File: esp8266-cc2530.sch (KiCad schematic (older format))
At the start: 34 parts, among them J1 CC2530_programmingHeader, J2 Conn_Coaxial, U1 WeMos_D1_mini, U2 AMS1117-3.3, U3 CC2530Fxxx, U4 RFX2401C, Y1 32.768kHz, Y2 32MHz

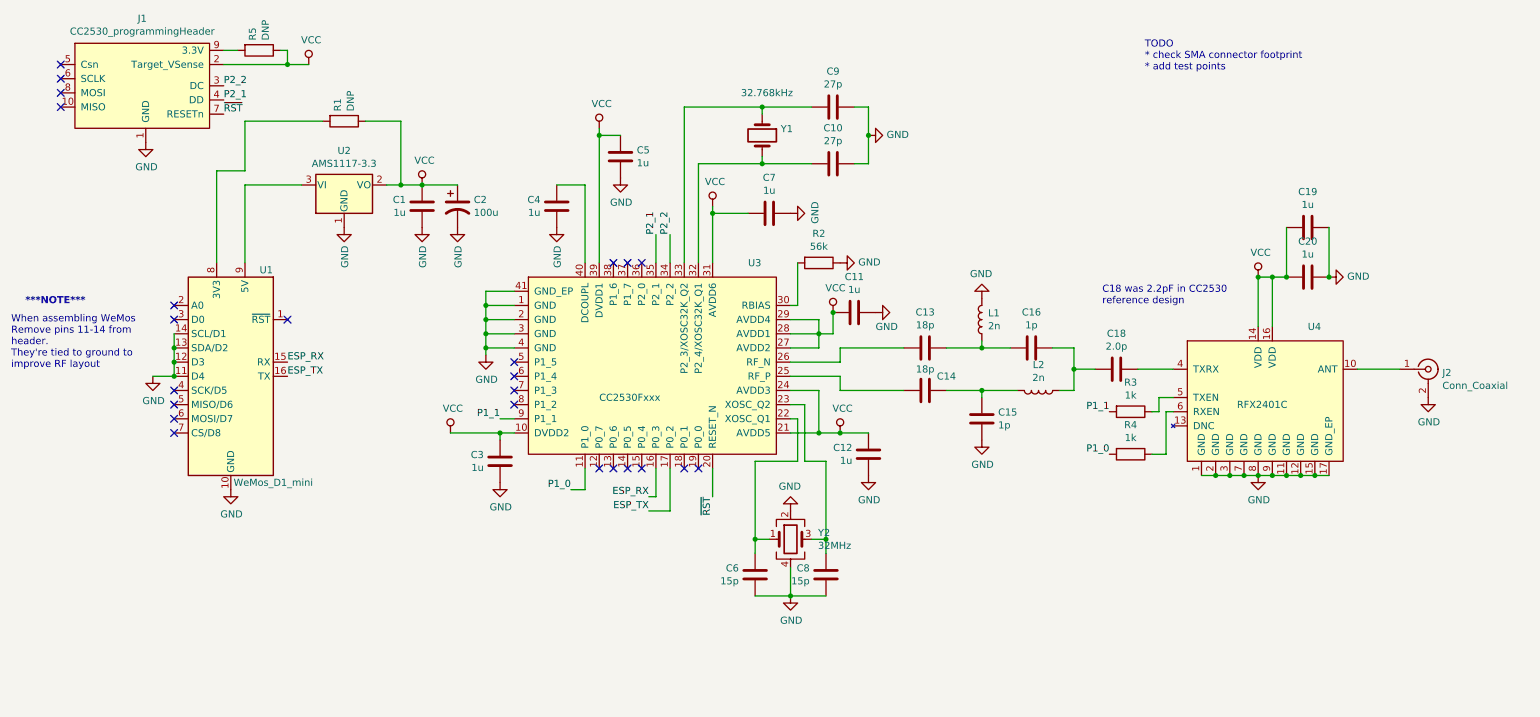
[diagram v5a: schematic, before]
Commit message: added usb connector, not routed yet
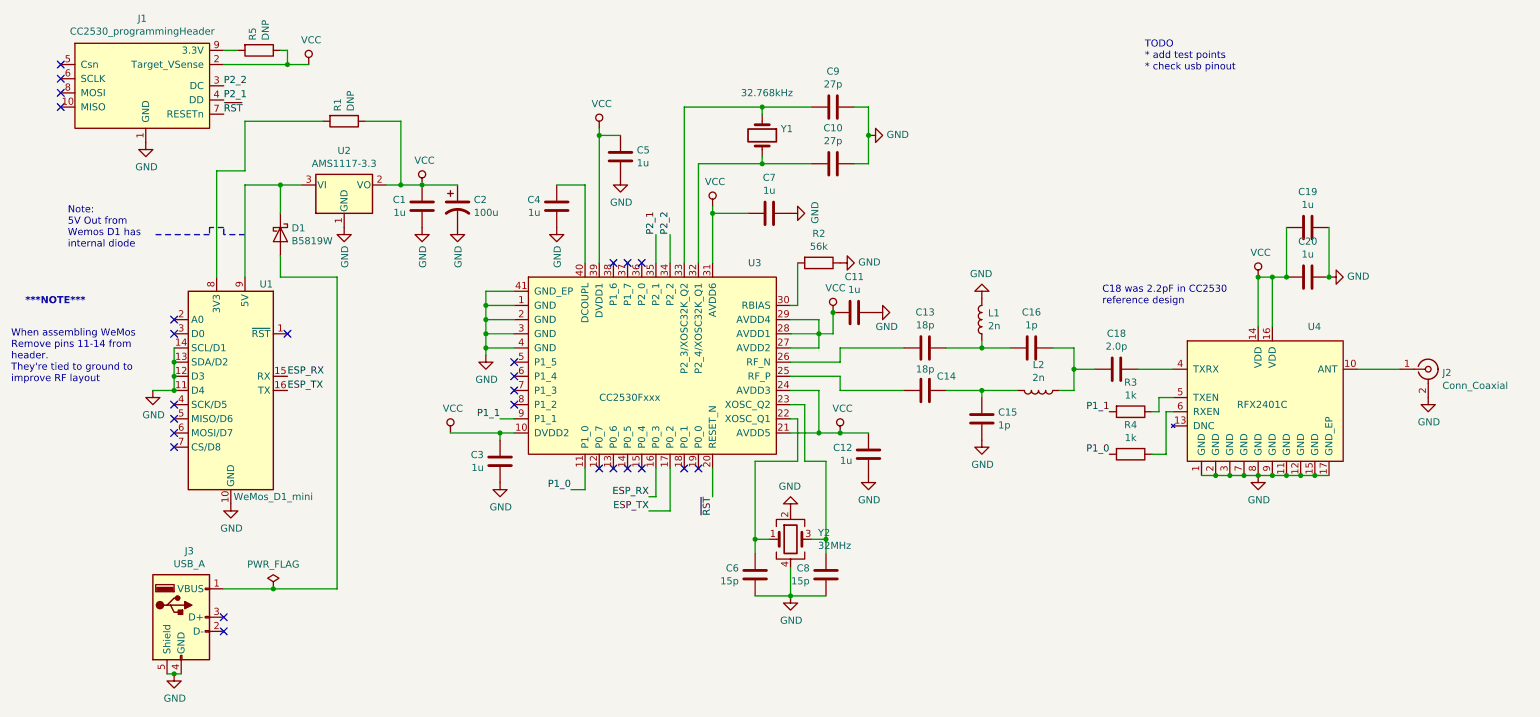
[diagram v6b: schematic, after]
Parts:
- added D1: B5819W, Diode_SMD:D_SOD-123, symbol projectLib:B5819W
- added J3: USB_A, esp8266-cc2530:Molex_48037-2200_USB-A, symbol Connector:USB_A
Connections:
- net GND: now also J3.4 (GND), J3.5 (Shield)
- net at U1.9 (5V), U2.3 (VI): now also D1.1 (K)
- new net: D1.2 (A), J3.1 (VBUS)
- no-connect marks 24 -> 26
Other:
- note added: "Note:\n5V Out from \nWemos D1 has \ninternal diode"
- note added: "TODO\n* add test points\n* check usb pinout"
- note removed: "TODO\n* check SMA connector footprint\n* add test points"
- moved on the sheet: U1
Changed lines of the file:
@@
 Connection ~ 9800 2400
 Text Notes 8500 950  0    50   ~ 0
-TODO\n* check SMA connector footprint\n* add test points
+TODO\n* add test points\n* check usb pinout
 $Comp
 L Device:C C3
@@
 Text Label 8250 3650 2    50   ~ 0
 P1_0
-$Comp
-L power:GND #PWR0129
-U 1 1 5EBADD70
-P 2050 3900
-F 0 "#PWR0129" H 2050 3650 50  0001 C CNN
-F 1 "GND" H 2055 3727 50  0000 C CNN
-F 2 "" H 2050 3900 50  0001 C CNN
-F 3 "" H 2050 3900 50  0001 C CNN
-	1    2050 3900
-	1    0    0    -1
-$EndComp
-Text Label 2450 3000 0    50   ~ 0
+Text Label 2450 3100 0    50   ~ 0
 ESP_RX
-Text Label 2450 3100 0    50   ~ 0
+Text Label 2450 3200 0    50   ~ 0
 ESP_TX
 $Comp
@@
 $EndComp
 Wire Wire Line
-	2150 1750 2150 2300
-Wire Wire Line
 	3000 1300 3250 1300
 Wire Wire Line
@@
 Wire Wire Line
 	3250 1750 3400 1750
-$Comp
-L projectLib:WeMos_D1_mini U1
-U 1 1 5EC6ED24
-P 2050 3100
-F 0 "U1" H 1800 3850 50  0000 C CNN
-F 1 "WeMos_D1_mini" H 1750 2350 50  0000 C CNN
-F 2 "esp8266-cc2530:WEMOS_D1_mini_smt" H 2050 1950 50  0001 C CNN
-F 3 "https://wiki.wemos.cc/products:d1:d1_mini#documentation" H 200 1950 50  0001 C CNN
-	1    2050 3100
-	-1   0    0    -1
-$EndComp
-NoConn ~ 2450 2700
-NoConn ~ 1650 2600
-NoConn ~ 1650 2700
-NoConn ~ 1650 3200
-NoConn ~ 1650 3300
-NoConn ~ 1650 3400
-NoConn ~ 1650 3500
 NoConn ~ 4750 2300
 NoConn ~ 4850 2300
@@
 NoConn ~ 5350 3750
 Wire Wire Line
-	2150 1750 2550 1750
+	2150 1750 2400 1750
 Wire Wire Line
 	2150 1300 2150 1650
 Wire Wire Line
 	2150 1650 1950 1650
-Wire Wire Line
-	1950 1650 1950 2300
 Wire Wire Line
 	2150 1300 2700 1300
@@
 L power:GND #PWR0121
 U 1 1 5EAE54B3
-P 1500 3100
-F 0 "#PWR0121" H 1500 2850 50  0001 C CNN
-F 1 "GND" H 1505 2927 50  0000 C CNN
-F 2 "" H 1500 3100 50  0001 C CNN
-F 3 "" H 1500 3100 50  0001 C CNN
-	1    1500 3100
-	1    0    0    -1
-$EndComp
-Wire Wire Line
-	1500 3100 1650 3100
-Wire Wire Line
-	1650 2800 1650 2900
-Connection ~ 1650 3100
-Connection ~ 1650 2900
+P 1500 3200
+F 0 "#PWR0121" H 1500 2950 50  0001 C CNN
+F 1 "GND" H 1505 3027 50  0000 C CNN
+F 2 "" H 1500 3200 50  0001 C CNN
+F 3 "" H 1500 3200 50  0001 C CNN
+	1    1500 3200
+	1    0    0    -1
+$EndComp
+Text Notes 600  2600 0    50   ~ 10
+***NOTE***
+Text Notes 500  3150 0    50   ~ 0
+When assembling WeMos\nRemove pins 11-14 from \nheader.  \nThey're tied to ground to\nimprove RF layout
+$Comp
+L Connector:USB_A J3
+U 1 1 5EB89E00
+P 1700 4800
+F 0 "J3" H 1757 5267 50  0000 C CNN
+F 1 "USB_A" H 1757 5176 50  0000 C CNN
+F 2 "esp8266-cc2530:Molex_48037-2200_USB-A" H 1850 4750 50  0001 C CNN
+F 3 "https://docs.rs-online.com/f411/0900766b812cbeb0.pdf" H 1850 4750 50  0001 C CNN
+	1    1700 4800
+	1    0    0    -1
+$EndComp
+Wire Wire Line
+	1600 5200 1650 5200
+$Comp
+L power:GND #PWR09
+U 1 1 5EB9A860
+P 1650 5200
+F 0 "#PWR09" H 1650 4950 50  0001 C CNN
+F 1 "GND" H 1655 5027 50  0000 C CNN
+F 2 "" H 1650 5200 50  0001 C CNN
+F 3 "" H 1650 5200 50  0001 C CNN
+	1    1650 5200
+	1    0    0    -1
+$EndComp
+Connection ~ 1650 5200
+Wire Wire Line
+	1650 5200 1700 5200
+Connection ~ 2400 1750
+Wire Wire Line
+	2400 1750 2550 1750
+$Comp
+L projectLib:B5819W D1
+U 1 1 5EBAD6F6
+P 2400 2100
+F 0 "D1" V 2354 2179 50  0000 L CNN
+F 1 "B5819W" V 2445 2179 50  0000 L CNN
+F 2 "Diode_SMD:D_SOD-123" H 2400 1925 50  0001 C CNN
+F 3 "https://datasheet.lcsc.com/szlcsc/Changjiang-Electronics-Tech-CJ-B5819W_C8598.pdf" H 2400 2100 50  0001 C CNN
+F 4 "C8598" H 2400 2100 50  0001 C CNN "LCSC"
+	1    2400 2100
+	0    1    1    0
+$EndComp
+Wire Wire Line
+	2400 1950 2400 1750
+NoConn ~ 1650 3600
+NoConn ~ 1650 3500
+NoConn ~ 1650 3400
+NoConn ~ 1650 3300
+NoConn ~ 1650 2800
+NoConn ~ 1650 2700
+Wire Wire Line
+	1500 3200 1650 3200
+$Comp
+L power:GND #PWR0129
+U 1 1 5EBADD70
+P 2050 4000
+F 0 "#PWR0129" H 2050 3750 50  0001 C CNN
+F 1 "GND" H 2055 3827 50  0000 C CNN
+F 2 "" H 2050 4000 50  0001 C CNN
+F 3 "" H 2050 4000 50  0001 C CNN
+	1    2050 4000
+	1    0    0    -1
+$EndComp
+NoConn ~ 2450 2800
 Wire Wire Line
 	1650 2900 1650 3000
 Connection ~ 1650 3000
 Wire Wire Line
+	1650 3100 1650 3200
+Wire Wire Line
 	1650 3000 1650 3100
-Text Notes 600  2600 0    50   ~ 10
-***NOTE***
-Text Notes 500  3050 0    50   ~ 0
-When assembling WeMos\nRemove pins 11-14 from \nheader.  \nThey're tied to ground to\nimprove RF layout
+Connection ~ 1650 3100
+Connection ~ 1650 3200
+$Comp
+L projectLib:WeMos_D1_mini U1
+U 1 1 5EC6ED24
+P 2050 3200
+F 0 "U1" H 1800 3950 50  0000 C CNN
+F 1 "WeMos_D1_mini" H 1750 2450 50  0000 C CNN
+F 2 "esp8266-cc2530:WEMOS_D1_mini_smt" H 2050 2050 50  0001 C CNN
+F 3 "https://wiki.wemos.cc/products:d1:d1_mini#documentation" H 200 2050 50  0001 C CNN
+	1    2050 3200
+	-1   0    0    -1
+$EndComp
+Wire Wire Line
+	2800 2400 2400 2400
+Wire Wire Line
+	2400 2400 2400 2250
+Wire Wire Line
+	2800 2400 2800 4600
+Wire Wire Line
+	2150 1750 2150 2400
+Wire Wire Line
+	1950 1650 1950 2400
+Wire Notes Line
+	2150 2100 2000 2100
+Wire Notes Line
+	2000 2100 2000 2050
+Wire Notes Line
+	2000 2050 1900 2050
+Wire Notes Line
+	1900 2050 1900 2100
+Wire Notes Line
+	1900 2100 1500 2100
+Text Notes 900  2200 0    50   ~ 0
+Note:\n5V Out from \nWemos D1 has \ninternal diode
+NoConn ~ 2000 4800
+NoConn ~ 2000 4900
+Wire Wire Line
+	2350 4600 2800 4600
+Wire Wire Line
+	2000 4600 2350 4600
+Connection ~ 2350 4600
+$Comp
+L power:PWR_FLAG #FLG0101
+U 1 1 5EC09F39
+P 2350 4600
+F 0 "#FLG0101" H 2350 4675 50  0001 C CNN
+F 1 "PWR_FLAG" H 2350 4773 50  0000 C CNN
+F 2 "" H 2350 4600 50  0001 C CNN
+F 3 "~" H 2350 4600 50  0001 C CNN
+	1    2350 4600
+	1    0    0    -1
+$EndComp
 $EndSCHEMATC

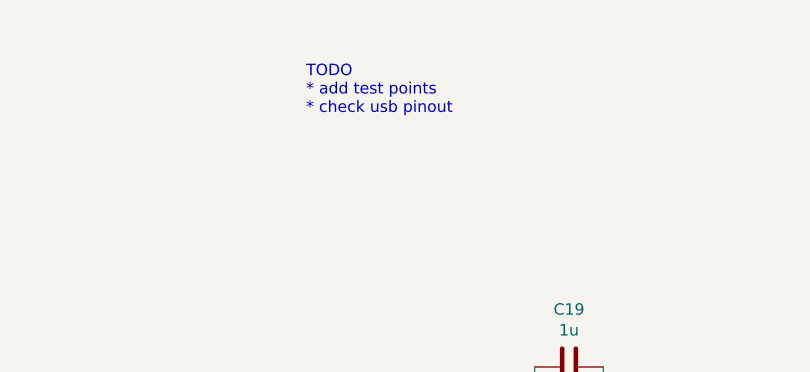
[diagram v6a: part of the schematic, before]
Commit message: verified usb connector pinout
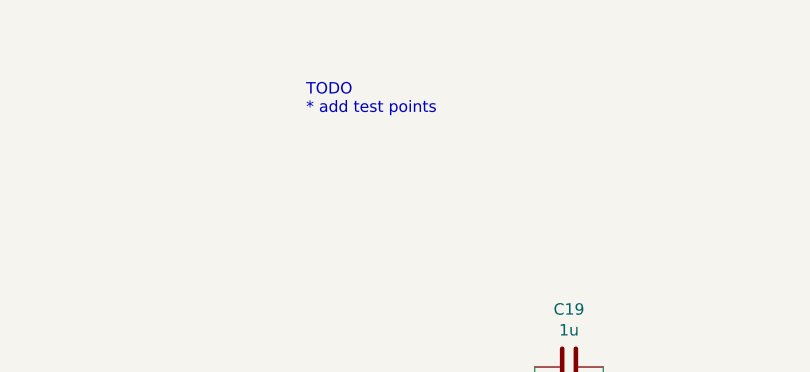
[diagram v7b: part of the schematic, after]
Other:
- note added: "TODO\n* add test points"
- note removed: "TODO\n* add test points\n* check usb pinout"
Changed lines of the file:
@@
 Connection ~ 9800 2400
 Text Notes 8500 950  0    50   ~ 0
-TODO\n* add test points\n* check usb pinout
+TODO\n* add test points
 $Comp
 L Device:C C3
